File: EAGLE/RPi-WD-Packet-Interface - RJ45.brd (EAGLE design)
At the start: 60 x 60 mm, 29 parts, among them IC1 TLC555, Q1 PTT, Q2 PTT-LED, Q3 DCD-LED

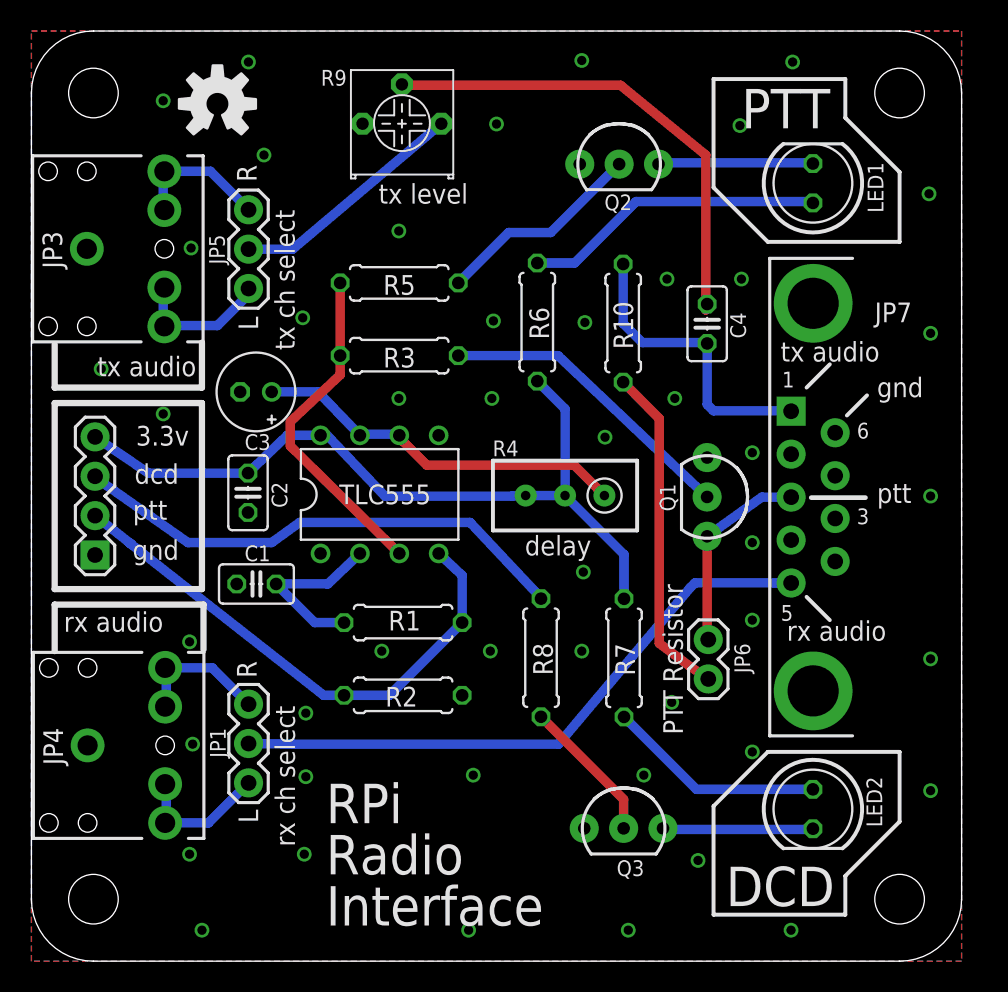
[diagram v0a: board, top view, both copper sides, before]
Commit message: Replace DB-9 files with RJ-45 version 1.0
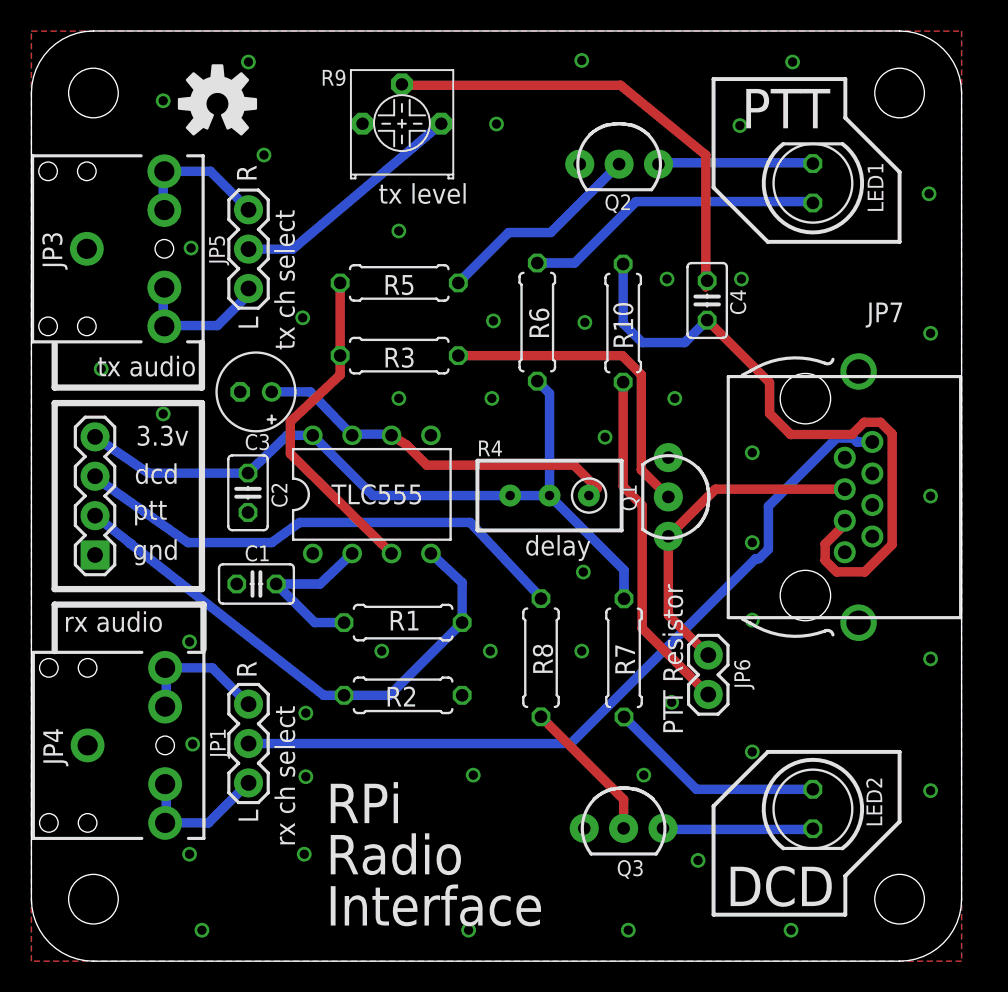
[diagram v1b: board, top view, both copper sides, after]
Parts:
- JP7: device SparkFun-Connectors:DB9 -> con-molex:0446200002
- moved Q1 2.50 mm to (41.6, 29.9)
- moved C4 1.50 mm to (44.1, 42.6)
- moved JP6 1.00 mm to (44.2, 19.7)
- moved R4 1.00 mm to (33.9, 30.0)
- moved IC1 0.50 mm to (22.5, 30.1)
- moved JP7 0.50 mm to (50.4, 29.9)
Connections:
- net GND: now also JP7.4, JP7.S@1, JP7.S@2
- net PTT: now also JP7.5; no longer JP7.3
- net RXAUDIO: now also JP7.8; no longer JP7.5
- net TXAUDIO: now also JP7.3; no longer JP7.1
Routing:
- net TXAUDIO: track 19.3 -> 42.7 mm
- net RXAUDIO: track 39.8 -> 50.1 mm
- net PTT: track 12.9 -> 21.4 mm
- net VCC: track 50.6 -> 49.0 mm
- net N$4: track 31.6 -> 30.1 mm
- net N$8: track 19.7 -> 20.9 mm
- net N$11: track 21.7 -> 22.4 mm
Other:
- board text removed: "1"
- board text removed: "3"
- board text removed: "5"
- board text removed: "6"

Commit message: RJ-45 rotation fix & silkscreen update
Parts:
- moved JP7 5.15 mm to (55.6, 30.1), turned to 90 degrees
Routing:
- net TXAUDIO: track 42.7 -> 26.6 mm
- net RXAUDIO: track 50.1 -> 44.7 mm
- net PTT: track 21.4 -> 26.2 mm
- net N$5: track 24.3 -> 23.6 mm
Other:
- board text added: "3"
- board text added: "4"
- board text added: "5"
- board text added: "6"
- board text added: "8"
- board text added: "Baofeng mobile microphone"
- board text added: "github.com/dirkbeer/RPi-WD-Packet-Interface"
- board text added: "version 1.0"
- board text removed: "github.com/jaymzx/RPi-WD-Packet-Interface"
- board text removed: "version 1.1 rev B"
